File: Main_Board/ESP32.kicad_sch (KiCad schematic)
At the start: 29 parts, among them J1 RESET, J2 MAIN_UART, Q1 2N7002, U1 W25Q128JVS, U2 ESP32-S3-MINI-1U

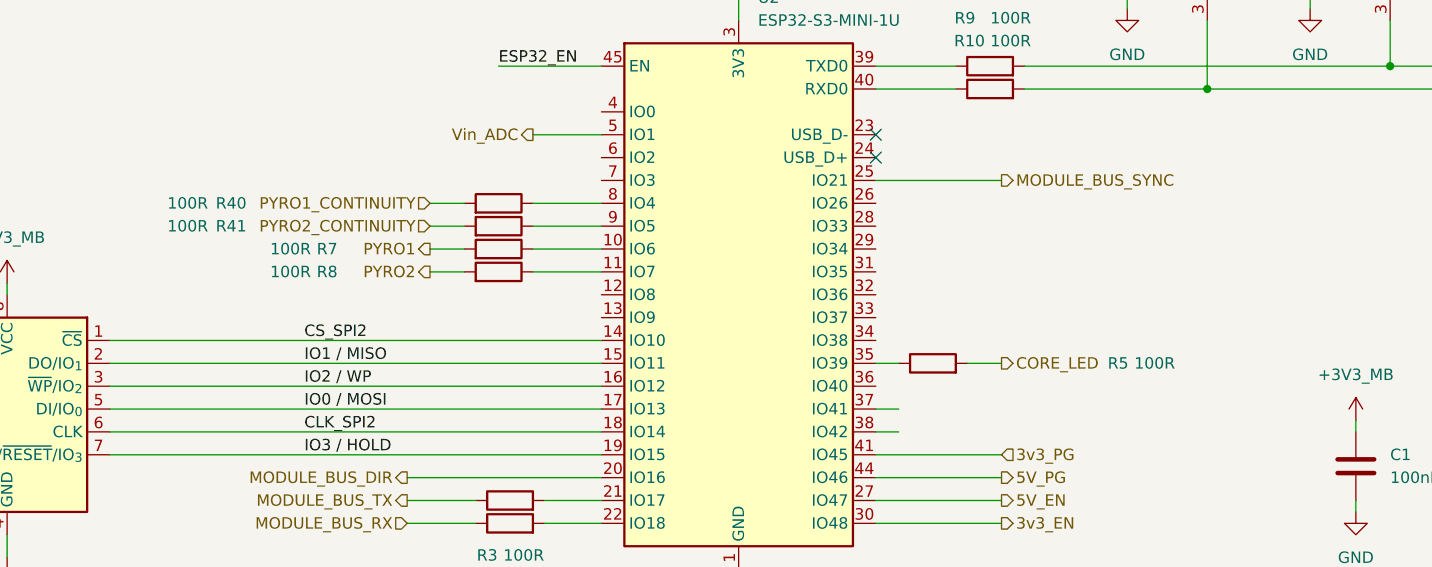
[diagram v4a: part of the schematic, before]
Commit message: Routing, repin pyro continuity to IO38
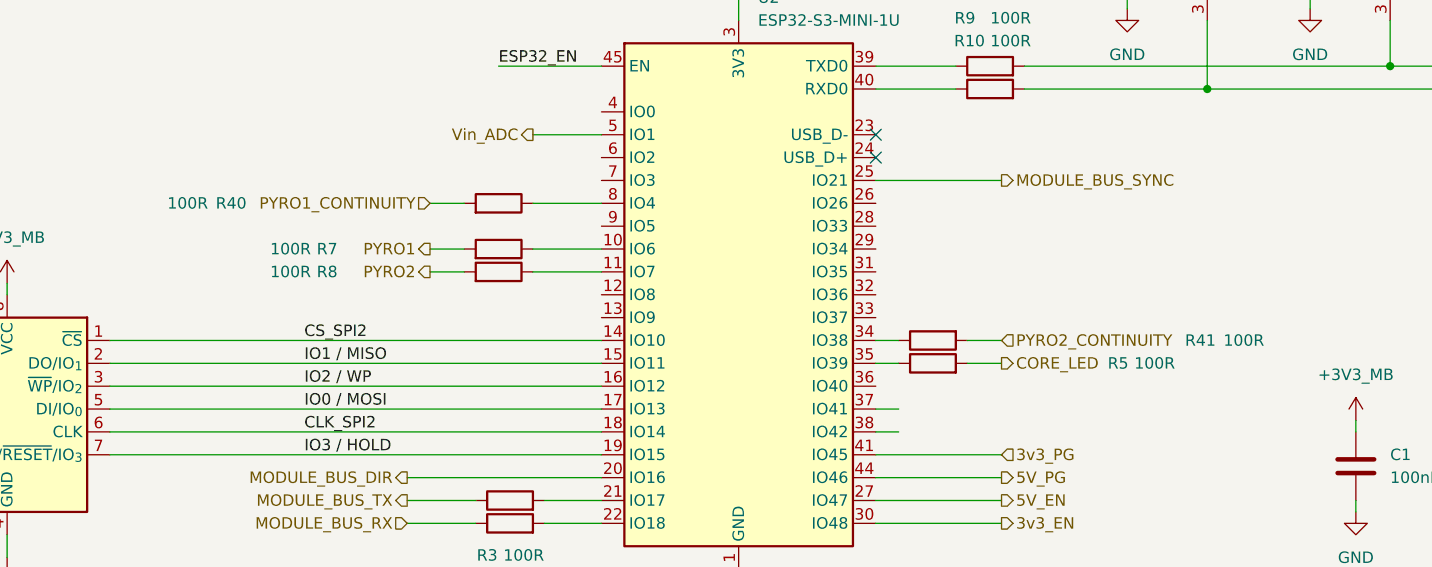
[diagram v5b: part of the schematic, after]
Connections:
- net at R41.1: now also U2.34 (IO38); no longer U2.9 (IO5)
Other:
- moved on the sheet: R41
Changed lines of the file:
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@@
 	(wire
 		(pts
-			(xy 106.68 58.42) (xy 110.49 58.42)
+			(xy 170.18 71.12) (xy 166.37 71.12)
 		)
 		(stroke
@@
 	(wire
 		(pts
+			(xy 158.75 71.12) (xy 156.21 71.12)
+		)
+		(stroke
+			(width 0)
+			(type default)
+		)
+	)
+	(wire
+		(pts
 			(xy 104.14 91.44) (xy 111.76 91.44)
 		)
@@
 		(pts
 			(xy 156.21 40.64) (xy 165.1 40.64)
-		)
-		(stroke
-			(width 0)
-			(type default)
-		)
-	)
-	(wire
-		(pts
-			(xy 118.11 58.42) (xy 125.73 58.42)
 		)
 		(stroke
@@
 	(hierarchical_label "PYRO2_CONTINUITY"
 		(shape input)
-		(at 106.68 58.42 180)
-		(effects
-			(font
-				(size 1.27 1.27)
-			)
-			(justify right)
+		(at 170.18 71.12 0)
+		(effects
+			(font
+				(size 1.27 1.27)
+			)
+			(justify left)
 		)
 	)
@@
 	(symbol
 		(lib_id "Device:R")
-		(at 114.3 58.42 270)
+		(at 162.56 71.12 90)
 		(mirror x)
 		(unit 1)
@@
 		(dnp no)
 		(property "Reference" "R41"
-			(at 84.582 58.42 90)
+			(at 192.278 71.12 90)
 			(show_name no)
 			(do_not_autoplace no)
@@
 		)
 		(property "Value" "100R"
-			(at 79.756 58.42 90)
+			(at 197.104 71.12 90)
 			(show_name no)
 			(do_not_autoplace no)
@@
 		)
 		(property "Footprint" "Resistor_SMD:R_0603_1608Metric"
-			(at 114.3 60.198 90)
+			(at 162.56 69.342 90)
 			(hide yes)
 			(show_name no)
@@
 		)
 		(property "Datasheet" ""
-			(at 114.3 58.42 0)
+			(at 162.56 71.12 0)
 			(hide yes)
 			(show_name no)
@@
 		)
 		(property "Description" "Resistor"
-			(at 114.3 58.42 0)
+			(at 162.56 71.12 0)
 			(hide yes)
 			(show_name no)
